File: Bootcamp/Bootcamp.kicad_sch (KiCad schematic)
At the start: 8 parts

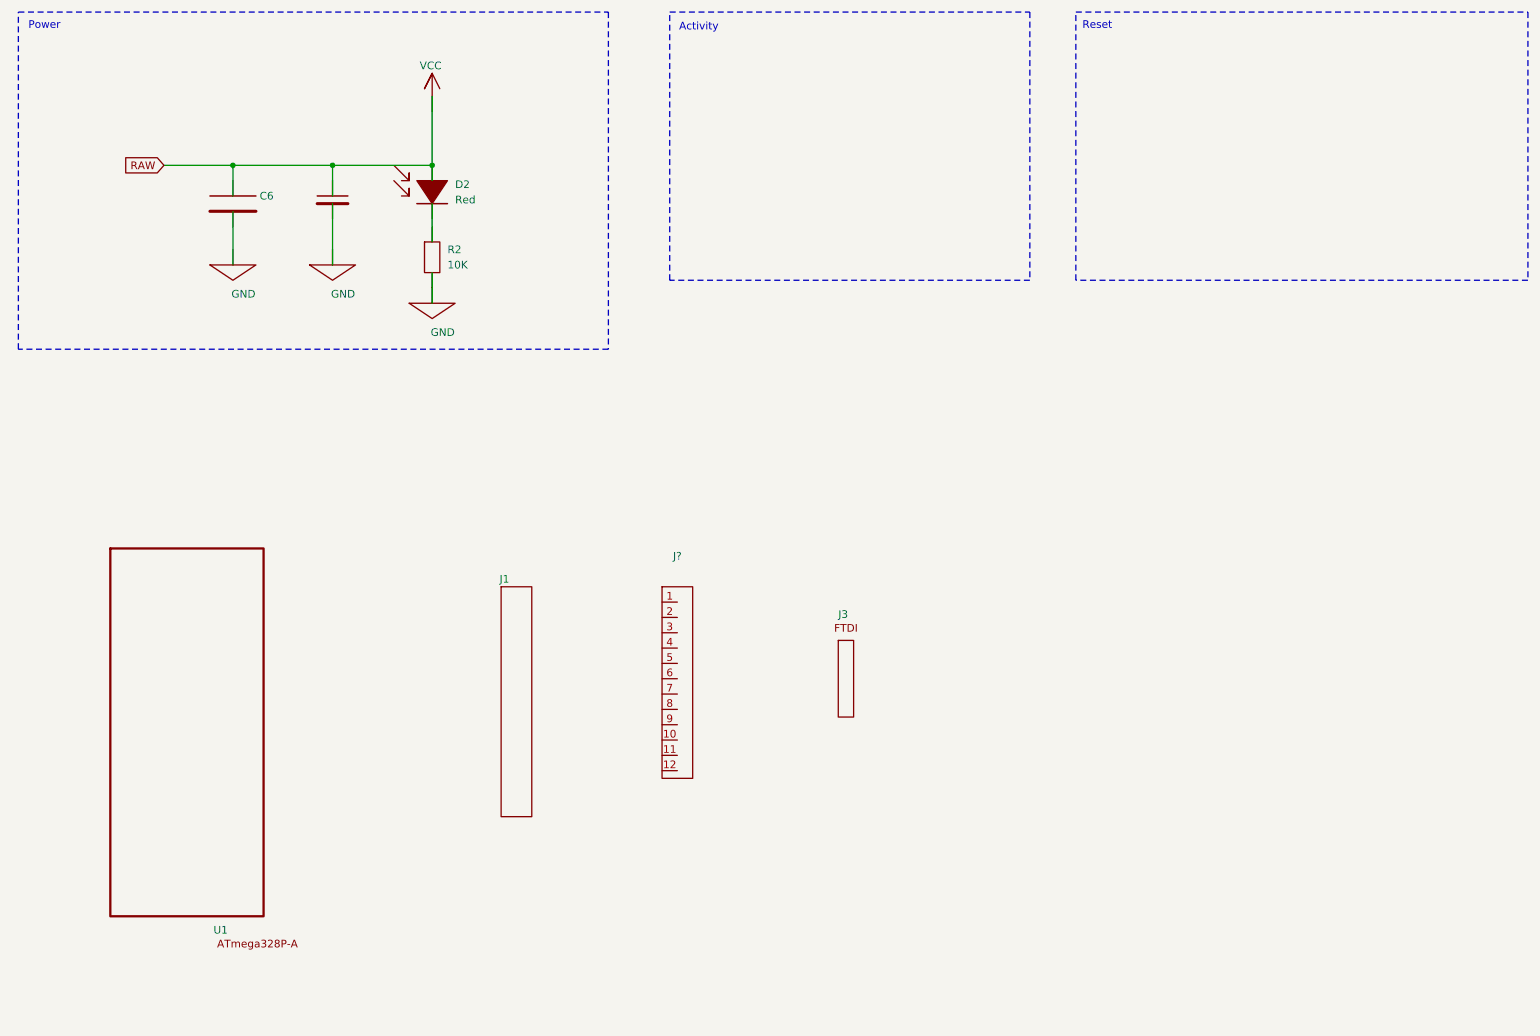
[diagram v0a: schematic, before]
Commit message: 2 errors missing schema
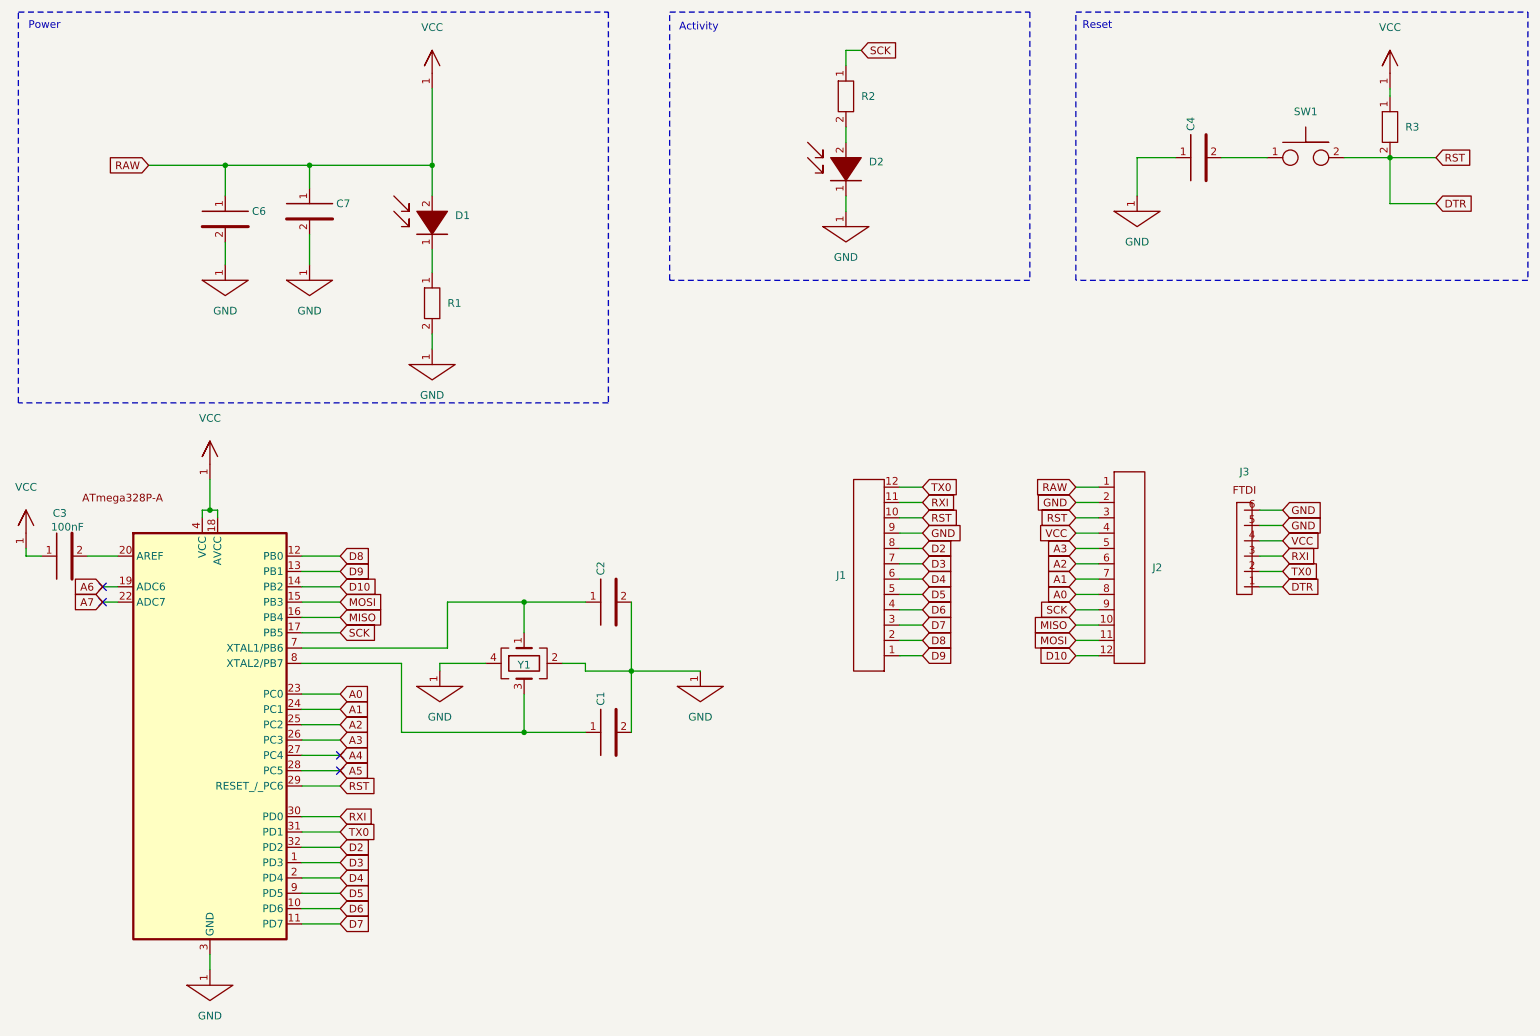
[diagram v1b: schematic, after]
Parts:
- removed J?: ~, symbol LibrairieBootcamp:Header_1x12
- added C1, C2, C4: (no value), symbol LibrairieBootcamp:Condensateur
- added C3: 100nF, symbol LibrairieBootcamp:Condensateur
- added D1: (no value), symbol LibrairieBootcamp:Led
- added J2: (no value), symbol LibrairieBootcamp:Header_1x12
- added R1, R3: (no value), symbol LibrairieBootcamp:Resistance
- added SW1: (no value), symbol LibrairieBootcamp:BoutonPoussoir
- added Y1: (no value), symbol LibrairieBootcamp:Quartz
- C6, C7, J1, J3, U1: value ~ -> (none)
- D2: value Red -> (none)
- R2: value 10K -> (none)
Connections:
- net GND: now also C6.2, C7.2, D2.1, J1.9, J3.5, J3.6, U1.21 (GND), U1.3 (GND), C1.2, C2.2, C4.1, J2.2, R1.2, Y1.2, Y1.4; no longer C6., C7., R2.
- removed net RAW: C6., C7., D2.
- new net: D1.1, R1.1
- new net: D2.2, R2.2
- new net: C4.2, SW1.1
- new net: C1.1, U1.8 (XTAL2/PB7), Y1.3
- new net: C3.2, U1.20 (AREF)
- new net: C2.1, U1.7 (XTAL1/PB6), Y1.1
- new net A0: J2.8, U1.23 (PC0)
- new net A1: J2.7, U1.24 (PC1)
- new net A2: J2.6, U1.25 (PC2)
- new net A3: J2.5, U1.26 (PC3)
- new net A4: U1.27 (PC4)
- new net A5: U1.28 (PC5)
- new net A6: U1.19 (ADC6)
- new net A7: U1.22 (ADC7)
- new net D10: J2.12, U1.14 (PB2)
- new net D2: J1.8, U1.32 (PD2)
- new net D3: J1.7, U1.1 (PD3)
- new net D4: J1.6, U1.2 (PD4)
- new net D5: J1.5, U1.9 (PD5)
- new net D6: J1.4, U1.10 (PD6)
- new net D7: J1.3, U1.11 (PD7)
- new net D8: J1.2, U1.12 (PB0)
- new net D9: J1.1, U1.13 (PB1)
- new net DTR: J1.10, J2.3, J3.1, R3.2, SW1.2, U1.29 (RESET_/_PC6)
- new net MISO: J2.10, U1.16 (PB4)
- new net MOSI: J2.11, U1.15 (PB3)
- new net RXI: J1.11, J3.3, U1.30 (PD0)
- new net SCK: J2.9, R2.1, U1.17 (PB5)
- new net TX0: J1.12, J3.2, U1.31 (PD1)
- new net VCC: C3.1, C6.1, C7.1, D1.2, J2.1, J2.4, J3.4, R3.1, U1.18 (AVCC), U1.4 (VCC), U1.6 (VCC)
- no-connect marks 0 -> 4

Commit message: fix errors
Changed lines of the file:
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@@
 	)
 	(junction
+		(at 58.42 185.42)
+		(diameter 0)
+		(color 0 0 0 0)
+	)
+	(junction
 		(at 254 50.8)
 		(diameter 0)
@@
 	)
 	(junction
+		(at 57.15 110.49)
+		(diameter 0)
+		(color 0 0 0 0)
+	)
+	(junction
 		(at 128.27 135.89)
 		(diameter 0)
@@
 	(wire
 		(pts
+			(xy 49.53 189.23) (xy 53.34 189.23)
+		)
+		(stroke
+			(width 0)
+			(type default)
+		)
+	)
+	(wire
+		(pts
 			(xy 254 58.42) (xy 254 50.8)
 		)
@@
 	(wire
 		(pts
+			(xy 57.15 110.49) (xy 54.61 110.49)
+		)
+		(stroke
+			(width 0)
+			(type default)
+		)
+	)
+	(wire
+		(pts
 			(xy 201.93 130.81) (xy 205.74 130.81)
 		)
@@
 	(wire
 		(pts
+			(xy 54.61 110.49) (xy 54.61 109.22)
+		)
+		(stroke
+			(width 0)
+			(type default)
+		)
+	)
+	(wire
+		(pts
 			(xy 201.93 107.95) (xy 205.74 107.95)
 		)
@@
 	(wire
 		(pts
+			(xy 58.42 185.42) (xy 53.34 185.42)
+		)
+		(stroke
+			(width 0)
+			(type default)
+		)
+	)
+	(wire
+		(pts
 			(xy 172.72 133.35) (xy 176.53 133.35)
 		)
@@
 	(wire
 		(pts
+			(xy 53.34 185.42) (xy 53.34 189.23)
+		)
+		(stroke
+			(width 0)
+			(type default)
+		)
+	)
+	(wire
+		(pts
 			(xy 172.72 120.65) (xy 176.53 120.65)
 		)
@@
 	)
 	(symbol
+		(lib_id "LibrairieBootcamp:PWR_FLAG")
+		(at 54.61 100.33 0)
+		(unit 1)
+		(body_style 1)
+		(exclude_from_sim no)
+		(in_bom no)
+		(on_board no)
+		(in_pos_files yes)
+		(dnp no)
+		(fields_autoplaced yes)
+		(property "Reference" "#FLG02"
+			(at 54.864 102.362 0)
+			(hide yes)
+			(show_name no)
+			(do_not_autoplace no)
+			(effects
+				(font
+					(size 1.27 1.27)
+				)
+			)
+		)
+		(property "Value" "PWR_FLAG"
+			(at 54.61 100.33 0)
+			(hide yes)
+			(show_name no)
+			(do_not_autoplace no)
+			(effects
+				(font
+					(size 1.27 1.27)
+				)
+			)
+		)
+		(property "Footprint" ""
+			(at 54.61 100.33 0)
+			(hide yes)
+			(show_name no)
+			(do_not_autoplace no)
+			(effects
+				(font
+					(size 1.27 1.27)
+				)
+			)
+		)
+		(property "Datasheet" ""
+			(at 54.61 100.33 0)
+			(hide yes)
+			(show_name no)
+			(do_not_autoplace no)
+			(effects
+				(font
+					(size 1.27 1.27)
+				)
+			)
+		)
+		(property "Description" ""
+			(at 54.61 100.33 0)
+			(hide yes)
+			(show_name no)
+			(do_not_autoplace no)
+			(effects
+				(font
+					(size 1.27 1.27)
+				)
+			)
+		)
+		(pin "1"
+		)
+		(instances
+			(project "Bootcamp"
+				(path "/6f598f59-8b55-4112-a884-030ae0f870a8"
+					(reference "#FLG02")
+					(unit 1)
+				)
+			)
+		)
+	)
+	(symbol
 		(lib_id "LibrairieBootcamp:BoutonPoussoir")
 		(at 240.03 50.8 0)
@@
 					(unit 1)
 				)
+			)
+		)
+	)
+	(symbol
+		(lib_id "LibrairieBootcamp:PWR_FLAG")
+		(at 49.53 180.34 0)
+		(unit 1)
+		(body_style 1)
+		(exclude_from_sim no)
+		(in_bom no)
+		(on_board no)
+		(in_pos_files yes)
+		(dnp no)
+		(fields_autoplaced yes)
+		(property "Reference" "#FLG01"
+			(at 49.784 182.372 0)
+			(hide yes)
+			(show_name no)
+			(do_not_autoplace no)
+			(effects
+				(font
+					(size 1.27 1.27)
+				)
+			)
+		)
+		(property "Value" "PWR_FLAG"
+			(at 49.53 180.34 0)
+			(hide yes)
+			(show_name no)
+			(do_not_autoplace no)
+			(effects
+				(font
+					(size 1.27 1.27)
+				)
+			)
+		)
+		(property "Footprint" ""
+			(at 49.53 180.34 0)
+			(hide yes)
+			(show_name no)
+			(do_not_autoplace no)
+			(effects
+				(font
+					(size 1.27 1.27)
+				)
+			)
+		)
+		(property "Datasheet" ""
+			(at 49.53 180.34 0)
+			(hide yes)
+			(show_name no)
+			(do_not_autoplace no)
+			(effects
+				(font
+					(size 1.27 1.27)
+				)
+			)
+		)
+		(property "Description" ""
+			(at 49.53 180.34 0)
+			(hide yes)
+			(show_name no)
+			(do_not_autoplace no)
+			(effects
+				(font
+					(size 1.27 1.27)
+				)
+			)
+		)
+		(pin "1"
+		)
+		(instances
+			(project "Bootcamp"
+				(path "/6f598f59-8b55-4112-a884-030ae0f870a8"
+					(reference "#FLG01")
+					(unit 1)
+				)
